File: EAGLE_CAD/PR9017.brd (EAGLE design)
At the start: 70 x 70 mm, 72 parts

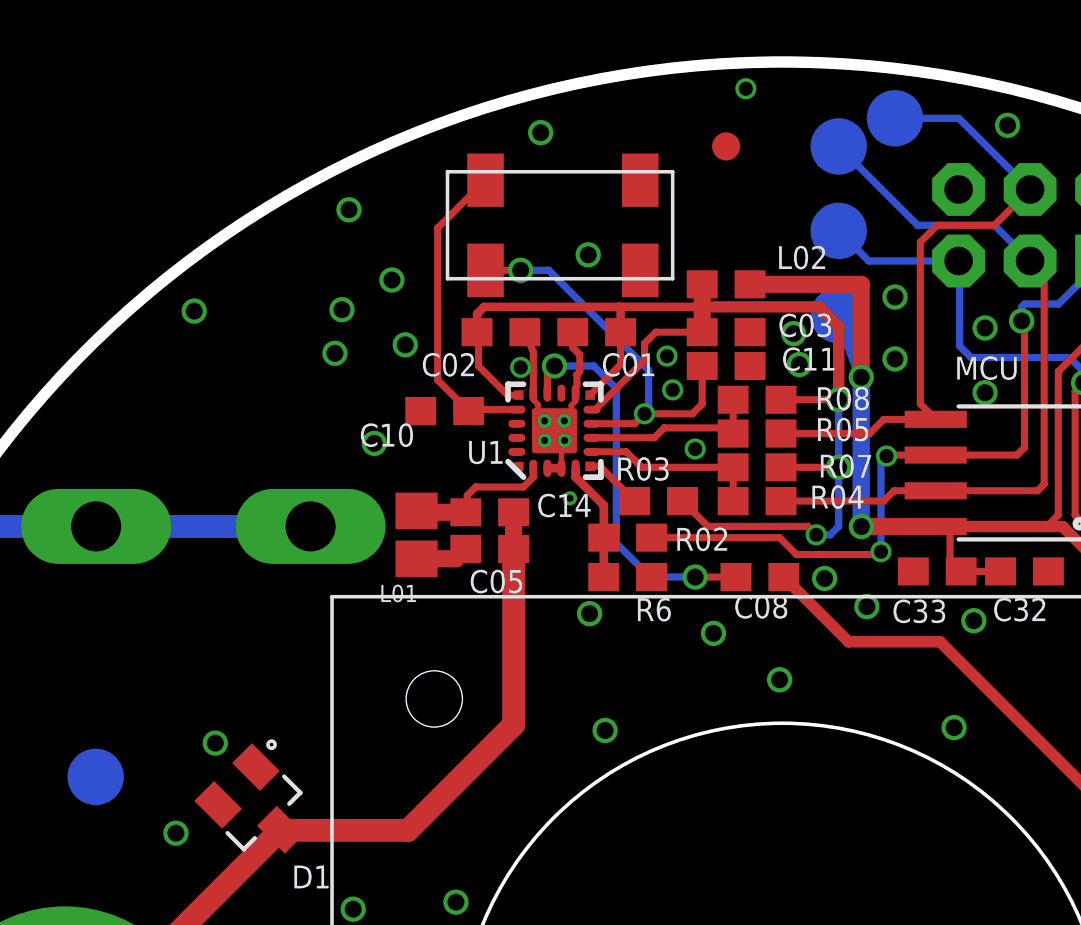
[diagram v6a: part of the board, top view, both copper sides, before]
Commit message: Layout Update
decoupling & crystal loading caps changes
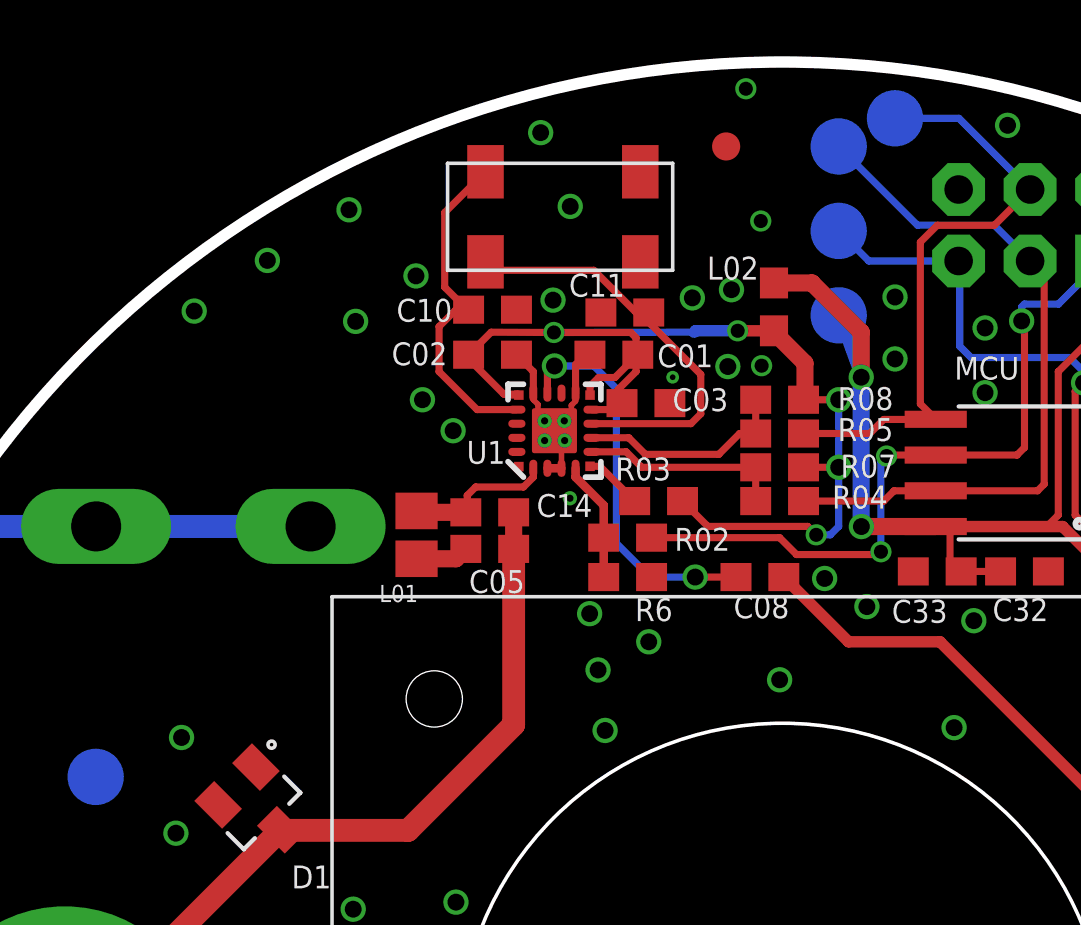
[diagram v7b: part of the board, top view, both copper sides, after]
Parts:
- moved C11 4.07 mm to (29.4, 61.1), turned to 180 degrees
- moved C10 3.98 mm to (24.7, 61.2), turned to 0 degrees
- moved C03 3.80 mm to (30.1, 57.9)
- moved L02 1.88 mm to (34.7, 61.3), turned to 270 degrees
- moved C01 1.01 mm to (29.0, 59.6)
- moved C02 0.85 mm to (24.7, 59.6)
- moved R04 0.80 mm to (34.9, 54.4)
- moved R05 0.80 mm to (34.9, 56.8)
- moved R07 0.80 mm to (34.9, 55.6)
- moved R08 0.80 mm to (34.9, 58.0)
- moved X1 0.30 mm to (27.2, 64.5)
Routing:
- net 3.3V: track 45.2 -> 40.1 mm, vias 3 -> 5
- net VCC: track 112.8 -> 110.9 mm
- net SDIO-L: track 6.44 -> 7.85 mm
- net N$10: track 11.1 -> 12.1 mm
- net GND: track 20.9 -> 19.9 mm, vias 72 -> 74
- net SDIO: track 22.8 -> 22.0 mm
- net SCLK-L: track 6.44 -> 7.24 mm
- net SCLK: track 26.3 -> 25.5 mm
- net N$1: track 14.4 -> 14.9 mm, vias 2 -> 0

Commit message: DRC Changes
DRC Changes
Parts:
- moved TP4 0.80 mm to (37.9, 17.7)
- moved C11 0.45 mm to (29.0, 61.3)
- moved C24 0.20 mm to (31.1, 10.3)
- moved C20 0.20 mm to (41.9, 7.10)
- moved C03 0.17 mm to (30.2, 58.0)
- moved R04 0.10 mm to (34.8, 54.4)
- moved R05 0.10 mm to (34.8, 56.8)
- moved R07 0.10 mm to (34.8, 55.6)
- moved R08 0.10 mm to (34.8, 58.0)
- moved C25 0.10 mm to (31.1, 7.80)
- moved C21 0.10 mm to (41.9, 9.60)
- moved C23 0.10 mm to (31.1, 9.10)
- moved R21 0.10 mm to (41.9, 8.30)
- moved X1 0.08 mm to (27.2, 64.6)
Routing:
- net N$5: track 9.04 -> 7.77 mm
- net VCC: track 110.9 -> 111.7 mm
- net GND: vias 74 -> 73
